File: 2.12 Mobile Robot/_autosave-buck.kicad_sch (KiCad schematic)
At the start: 17 parts, among them SW4 SW_PWR, U4 POWER_IN, U5 TPS564208DDCT

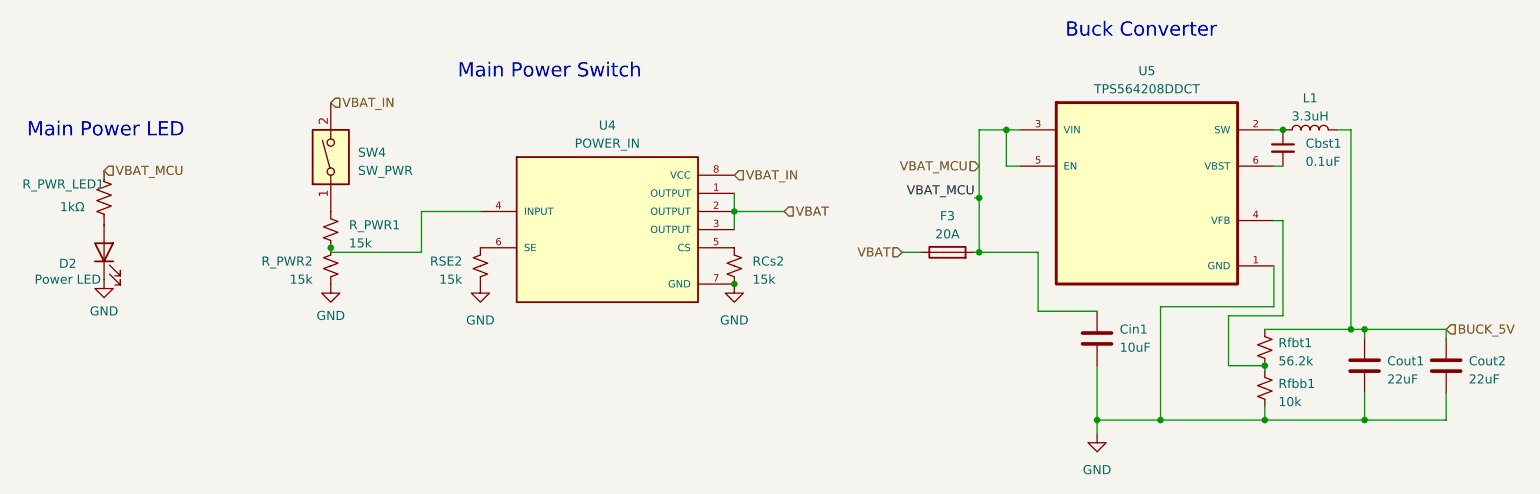
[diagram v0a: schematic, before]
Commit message: Renamed stuff
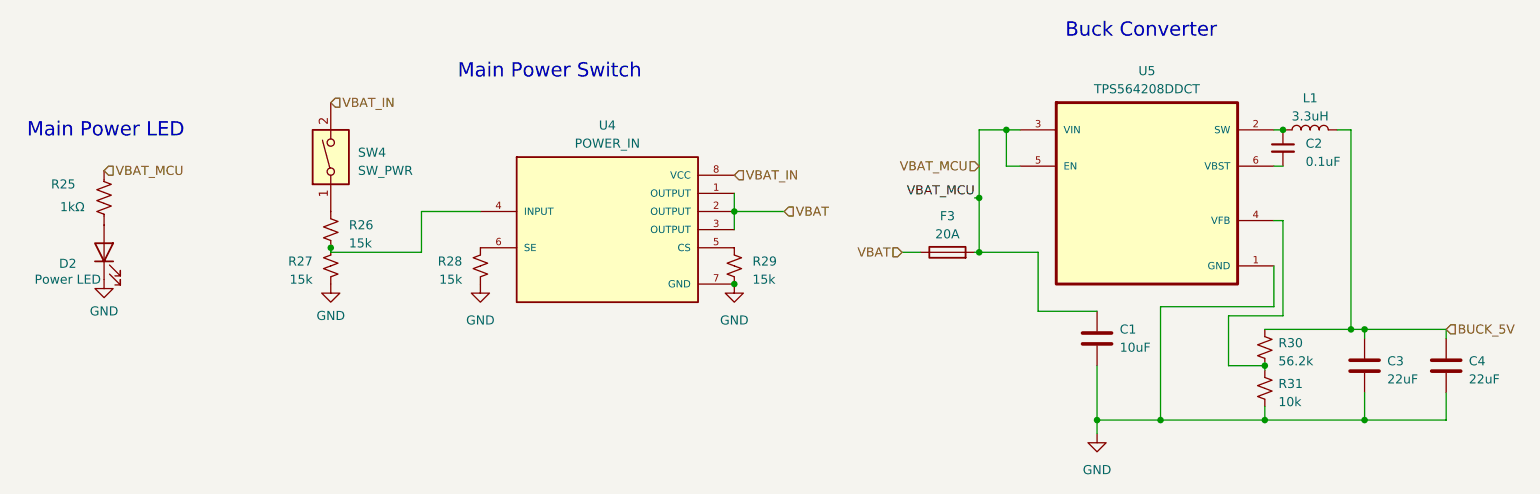
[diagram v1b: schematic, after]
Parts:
- C1: renamed from Cin1; Name (none) -> Cin1
- C2: renamed from Cbst1; Name (none) -> Cbst1
- C3: renamed from Cout1; Name (none) -> Cout1
- C4: renamed from Cout2; Name (none) -> Cout2
- R28: renamed from RSE2; Name (none) -> RSE2
- R29: renamed from RCs2; Name (none) -> RCs2
- R30: renamed from Rfbt1; Name (none) -> Rfbt1
- R31: renamed from Rfbb1; Name (none) -> Rfbb1
- renumbered R_PWR_LED1 to R25, R_PWR1 to R26, R_PWR2 to R27
